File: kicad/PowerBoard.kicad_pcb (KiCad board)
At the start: 2 copper layers, 150 x 150 mm, 185 parts, among them IC1 LT1910ES8#PBF, IC2 LT1910ES8#PBF, IC3 LT1910ES8#PBF, IC4 LT1910ES8#PBF, IC5 LT1910ES8#PBF, IC7 MAX17541GATB+T, J1 XT90, J10 XT90, J11 XT90, J12 XT90, J13 XT90, J14 DEAN_T, J15 DEAN_T, J16 DEAN_T, J17 DEAN_T, J18 DEAN_T, J19 DEAN_T, J2 DEAN_T, J20 XT60, J21 XT60, J22 XT60, J23 XT60, J24 XT60, J25 XT60, J26 XT60, J27 XT60, J28 XT60, J29 XT60, J3 XT60, J30 XT60, J31 XT60, J32 XT30, J33 XT30, J34 XT30, J35 XT30, J36 XT30, J37 XT30, J38 XT30, J39 XT30, J4 XT30, J40 XT30, J41 XT60, J42 DEAN_T, J43 DEAN_T, J44 XT60, J45 XT60, J46 XT60, J47 XT30, J48 XT30, J5 Conn_01x02, J6 XT90, J7 XT90, J8 XT90, J9 XT90, Q1 IRFS7530TRL7PP, Q2 IRFS7437TRLPBF, Q3 IRFS7437TRLPBF, Q4 IRFS7437TRLPBF, Q5 IRFS7437TRLPBF, U1 Pico, U2 INA238, U3 INA238, U4 INA238, U5 INA238, U6 INA238

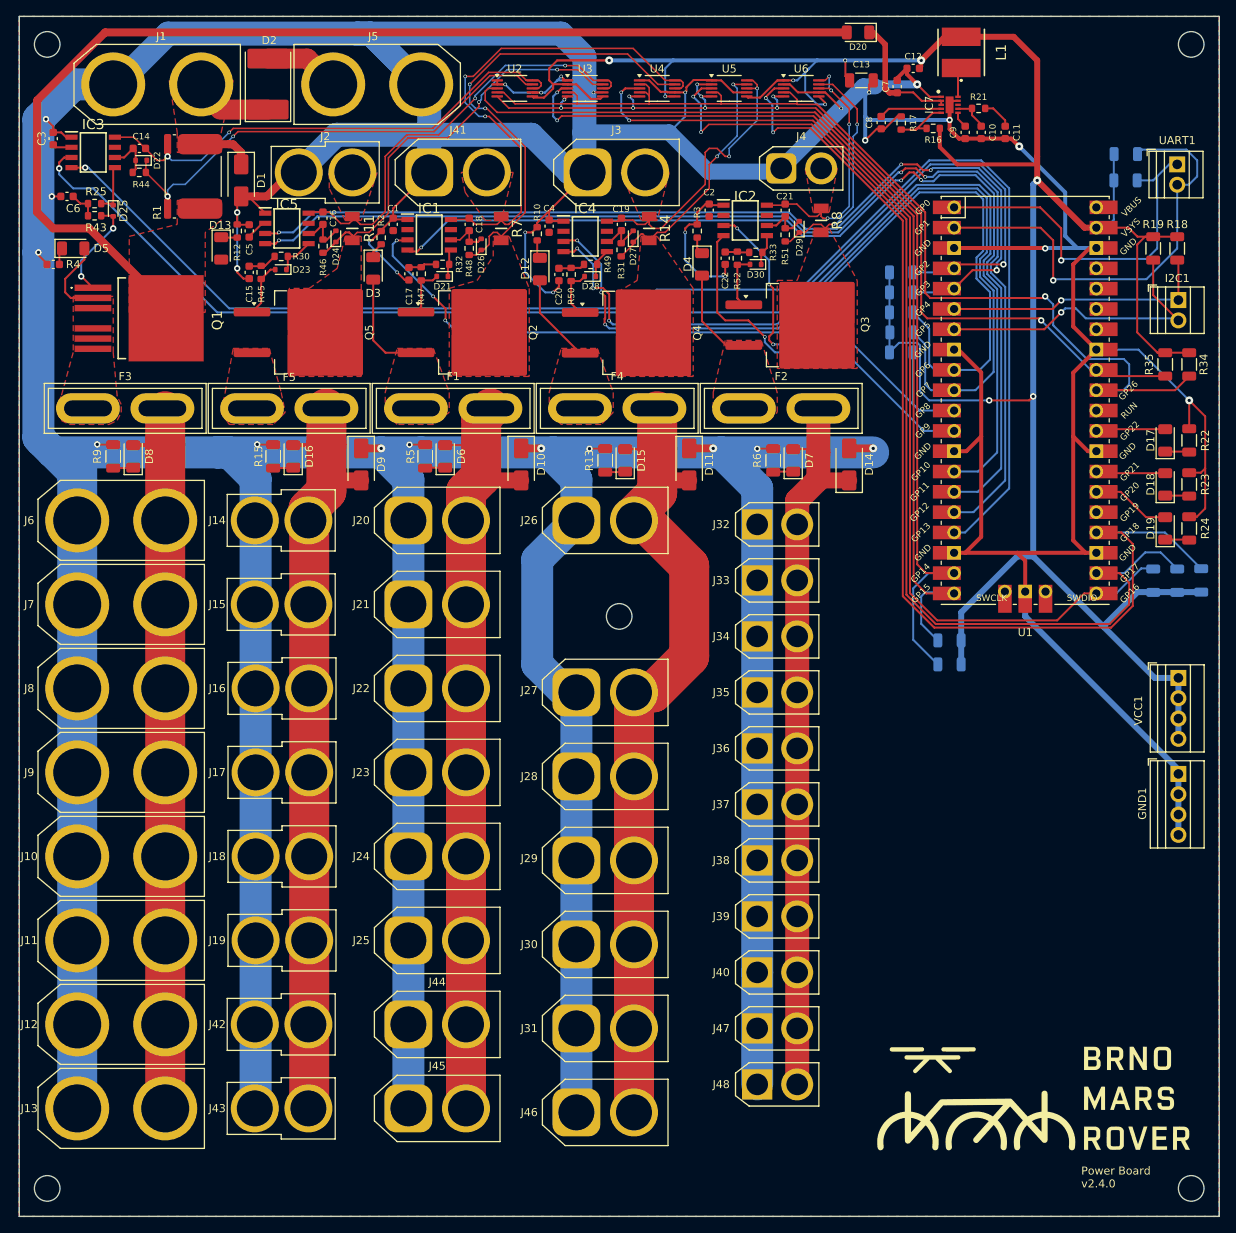
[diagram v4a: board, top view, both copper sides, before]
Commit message: rework the 5V switching
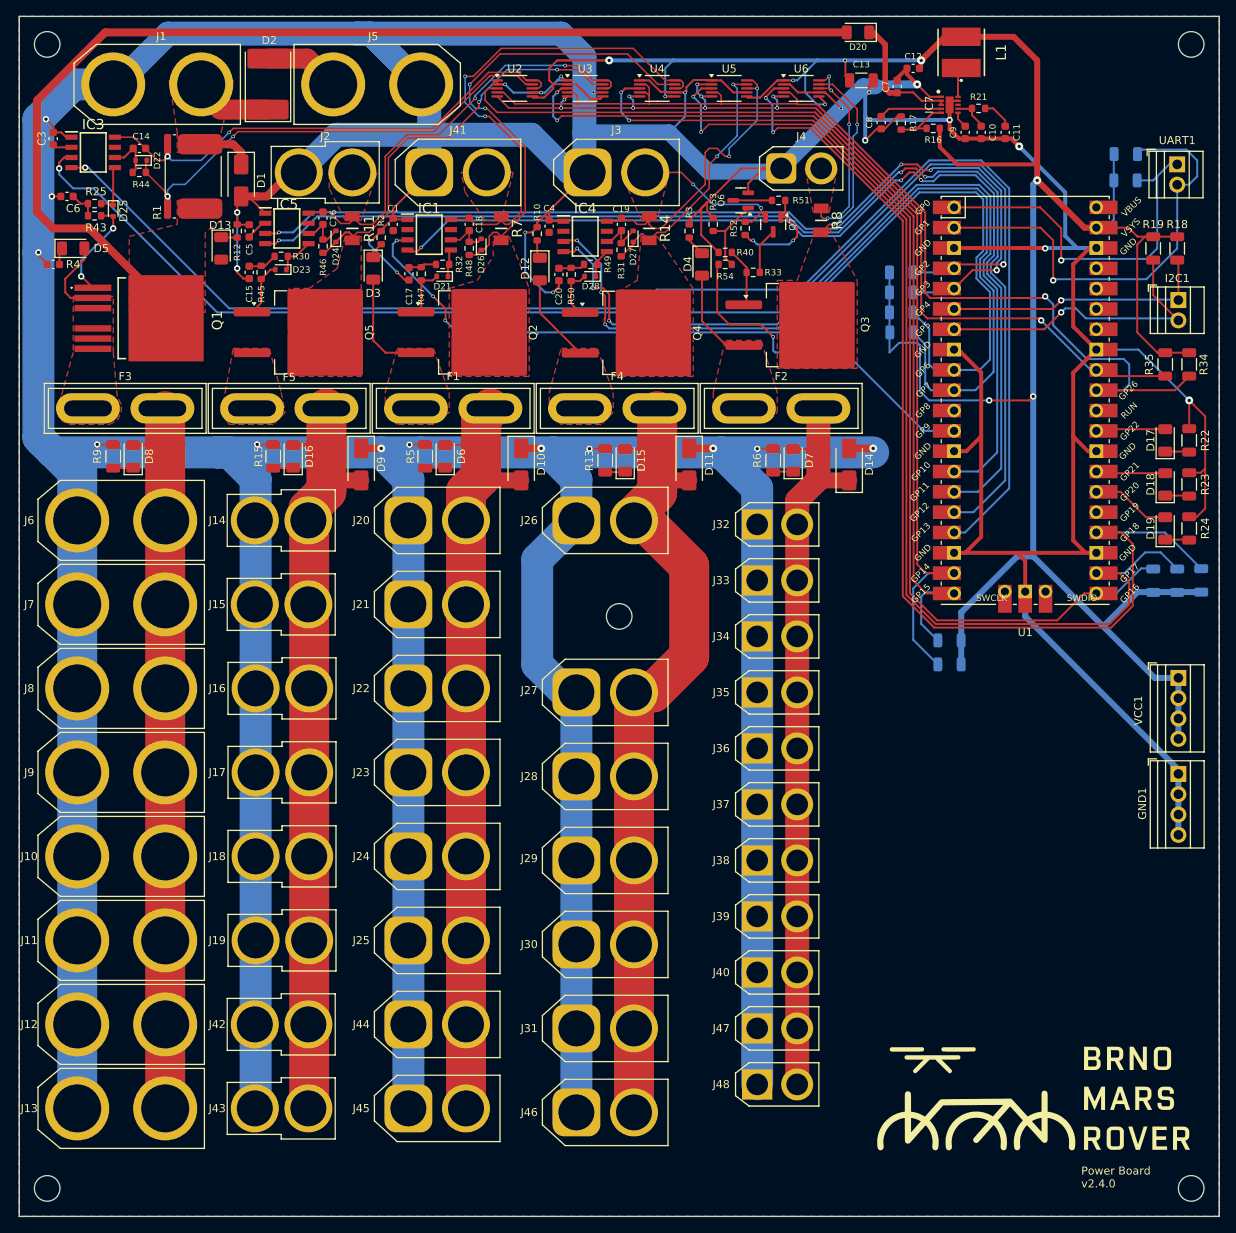
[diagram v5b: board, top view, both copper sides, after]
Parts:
- removed C2, C21, C22: 1u, Capacitor_SMD:C_0603_1608Metric
- removed D29, D30: 1N4148WT, Diode_SMD:D_SOD-523
- removed IC2: LT1910ES8#PBF, SamacSys_Parts:SOIC127P599X175-8N
- added Q6: BC818, Package_TO_SOT_SMD:SOT-23, F.Cu at (115.4, 41.0)
- added Q7: BC807, Package_TO_SOT_SMD:SOT-23, F.Cu at (119.5, 44.0)
- added R53: 100k, Resistor_SMD:R_0603_1608Metric, F.Cu at (112.0, 44.0)
- added R54: 100k, Resistor_SMD:R_0603_1608Metric, F.Cu at (113.5, 49.0)
- R40: value 5K -> 100k; footprint Resistor_SMD:R_1206_3216Metric -> Resistor_SMD:R_0603_1608Metric; moved to F.Cu
- R51: value 10k -> 100k
- moved R40 25.3 mm to (113.5, 47.5)
- moved R51 4.38 mm to (120.2, 41.0), turned to 0 degrees
- moved R52 3.86 mm to (116.0, 44.5), turned to 90 degrees
- moved R33 2.52 mm to (117.0, 50.0)
- moved R3 1.00 mm to (109.0, 44.8)
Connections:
- Q3 pad 1: /Q3-G -> Net-(Q3-G)
- R33 pad 1: Net-(C22-Pad2) -> Net-(Q3-G)
- R33 pad 2: /IC2-G -> Net-(Q7-C)
- R40 pad 1: VCC -> GND
- R40 pad 2: FAULT_5V -> Net-(Q3-G)
- R51 pad 1: /IC2-SENSE -> Net-(Q6-C)
- R51 pad 2: CURR_5- -> Net-(Q7-B)
- R52 pad 1: Net-(C22-Pad2) -> Net-(Q7-B)
- R52 pad 2: /Q3-G -> CURR_4+
- U1 pad 11: FAULT_5V -> unconnected-(U1-GPIO8-Pad11)_1
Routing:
- net FAULT_5V: track 52.3 -> 0.00 mm, vias 3 -> 0
- net CURR_4+: track 37.8 -> 58.0 mm, vias 2 -> 4
- net Net-(Q7-B): track 0.00 -> 13.3 mm, vias 0 -> 2
- net GND: track 1203.5 -> 1215.6 mm, vias 33 -> 31
- net Net-(Q6-B): track 0.00 -> 10.1 mm
- net CURR_5+: track 34.0 -> 26.4 mm
- net Net-(Q3-G): track 0.00 -> 7.64 mm
- net /Q3-G: track 6.94 -> 0.00 mm
- net /IC2-SENSE: track 6.50 -> 0.00 mm
- net CURR_5-: track 29.9 -> 23.8 mm
- net Net-(Q7-C): track 0.00 -> 5.76 mm
- net Net-(Q6-C): track 0.00 -> 4.85 mm
- net /IC2-G: track 3.89 -> 0.00 mm
- net EN_5V: track 46.1 -> 42.8 mm
- net Net-(C22-Pad2): track 3.06 -> 0.00 mm

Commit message: Generate gerber production files
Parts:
- removed D20: D, Diode_SMD:D_1206_3216Metric
- removed J5: Conn_01x02, SamacSys_Parts:XT90
- added Q8: MJD44H11, Package_TO_SOT_SMD:TO-252-2, F.Cu at (67.5, 25.0)
- added R55: 2k7, Resistor_SMD:R_1206_3216Metric, F.Cu at (77.5, 27.5)
- added TP1.1: TestPoint, TestPoint:TestPoint_Pad_1.0x1.0mm, F.Cu at (55.0, 27.5)
- added TP1.2: TestPoint, TestPoint:TestPoint_Pad_1.0x1.0mm, F.Cu at (55.0, 22.5)
- added TP1.3: TestPoint, TestPoint:TestPoint_Pad_1.0x1.0mm, F.Cu at (57.5, 27.5)
- added TP2.1: TestPoint, TestPoint:TestPoint_Pad_1.0x1.0mm, F.Cu at (57.5, 22.5)
- added TP2.2: TestPoint, TestPoint:TestPoint_Pad_1.0x1.0mm, F.Cu at (60.8, 49.6)
- added TP3.1: TestPoint, TestPoint:TestPoint_Pad_1.0x1.0mm, F.Cu at (135.0, 30.0)
- added TP3.2: TestPoint, TestPoint:TestPoint_Pad_1.0x1.0mm, F.Cu at (148.2, 25.0)
- added TP3.3: TestPoint, TestPoint:TestPoint_Pad_1.0x1.0mm, F.Cu at (150.7, 25.0)
- added TP3.4: TestPoint, TestPoint:TestPoint_Pad_1.0x1.0mm, F.Cu at (145.0, 27.9)
- added TP4.1: TestPoint, TestPoint:TestPoint_Pad_1.0x1.0mm, F.Cu at (60.0, 22.5)
- added TP4.2: TestPoint, TestPoint:TestPoint_Pad_1.0x1.0mm, F.Cu at (60.0, 27.5)
- added TP4.3: TestPoint, TestPoint:TestPoint_Pad_1.0x1.0mm, F.Cu at (145.0, 37.5)
- added TP4.4: TestPoint, TestPoint:TestPoint_Pad_1.0x1.0mm, F.Cu at (142.5, 37.5)
- added TP5.1: TestPoint, TestPoint:TestPoint_Pad_1.0x1.0mm, F.Cu at (81.5, 49.8)
- added TP6.1: TestPoint, TestPoint:TestPoint_Pad_1.0x1.0mm, F.Cu at (100.0, 50.0)
- C9: value 5.5nF -> 5.6nF
- D1: value SMAJ43A -> SMAJ40A
- D2: value D -> BZX84C39; footprint Diode_SMD:D_3220_8050Metric -> Package_TO_SOT_SMD:SOT-23
- Q6: value BC818 -> BC817
- R33: value 100k -> 1k
- R36, R37, R38, R39: value 5K -> 4k7
- R51: value 100k -> 680
- R52: value 100k -> 470
- R54: value 100k -> 4.7k
- moved D2 24.0 mm to (80.0, 22.5), turned to -90 degrees
- moved R17 4.65 mm to (140.0, 32.5), turned to 0 degrees
- moved R21 4.05 mm to (149.2, 29.6)
- moved R16 3.04 mm to (140.0, 35.0)
- moved C10 2.00 mm to (147.5, 32.5)
- moved C11 1.50 mm to (150.0, 32.5)
- moved C9 1.50 mm to (145.0, 32.5)
- moved D13 0.50 mm to (50.5, 47.5)
- moved Q5 0.50 mm to (62.5, 57.5)
- turned D14 to -90 degrees
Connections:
- C8 pad 1: Net-(IC7-VCC) -> Net-(IC7-FB)
- D14 pad 1: 5V_2 -> GND
- D14 pad 2: GND -> 5V_2
- D2 pad 1: +42V -> GND
- D2 pad 2: Net-(D2-A) -> unconnected-(D2-NC-Pad2)
- IC7 pad 4: Net-(IC7-VCC) -> Net-(IC7-FB)
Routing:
- net Net-(IC7-EN/UVLO): track 16.3 -> 76.4 mm
- net 42_SHUNT: track 141.3 -> 101.8 mm
- net CURR_2+: track 57.0 -> 94.1 mm, vias 2 -> 3
- net /IC3-G: track 6.37 -> 36.7 mm, vias 0 -> 2
- net SCL1: track 119.4 -> 146.8 mm
- net Net-(D13-A): track 2.51 -> 15.7 mm
- net CURR_1-: track 60.2 -> 72.7 mm
- net Net-(D2-K): track 0.00 -> 11.7 mm
- net CURR_1+: track 63.1 -> 73.7 mm
- net Net-(D2-A): track 9.49 -> 0.00 mm
- net Net-(IC7-VCC): track 7.89 -> 0.00 mm
- net SDA1: track 132.1 -> 139.9 mm
- net Net-(IC7-FB): track 7.26 -> 13.9 mm
- net Net-(IC7-SS): track 2.05 -> 7.68 mm, vias 0 -> 2
- net Net-(IC7-LX): track 3.77 -> 9.22 mm
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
